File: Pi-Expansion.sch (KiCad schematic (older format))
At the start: 21 parts, among them J1 RPi_GPIO, J2 MMCX_H, J3 PINHEADER_2X2_SMD, P1 BATT, U1 A2200-A, U2 Racom R-78B5.0-1.5L

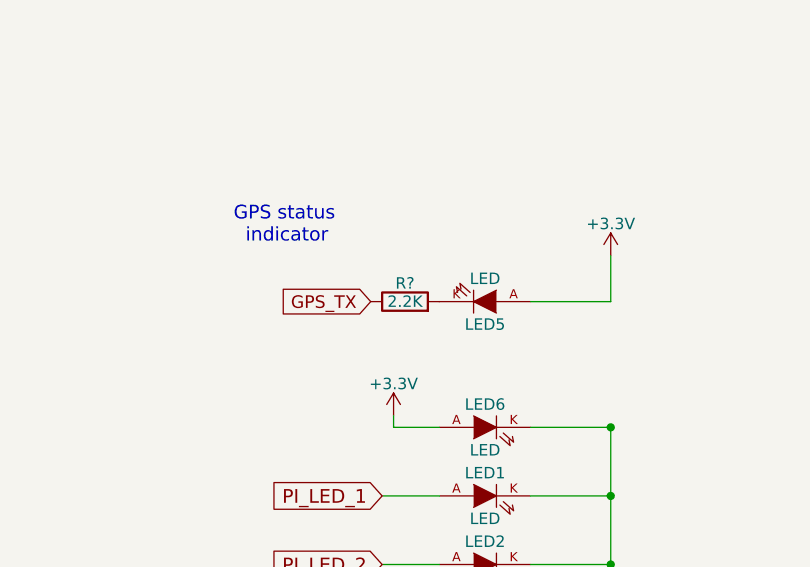
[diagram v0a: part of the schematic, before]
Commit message: Final version sent to fab, retraced GPS_TX to fix net issue between 2k2 resistor and pi header
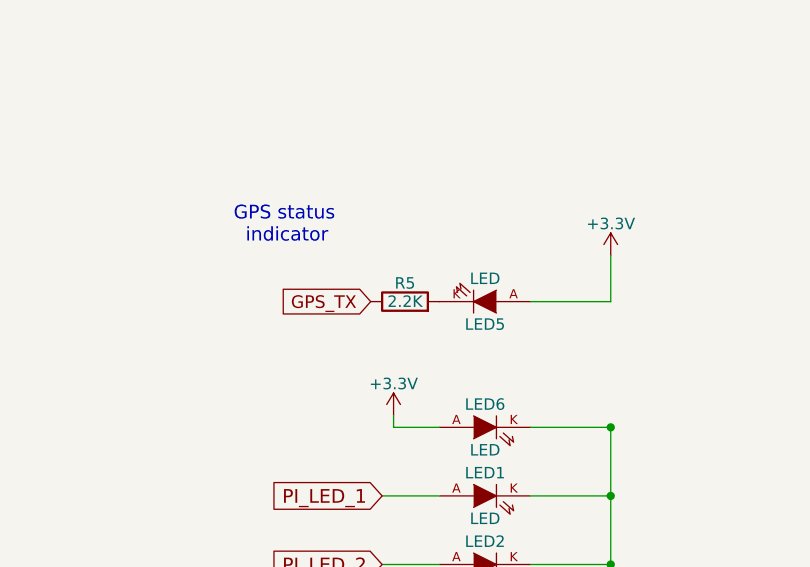
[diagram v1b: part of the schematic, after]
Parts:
- gave numbers to parts that had none: 1
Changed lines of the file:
@@
 $EndComp
 $Comp
-L GND #PWR01
+L GND #PWR18
 U 1 1 56C02961
 P 10850 5650
-F 0 "#PWR01" H 10850 5400 50  0001 C CNN
+F 0 "#PWR18" H 10850 5400 50  0001 C CNN
 F 1 "GND" H 10850 5500 50  0000 C CNN
 F 2 "" H 10850 5650 50  0000 C CNN
@@
 $EndComp
 $Comp
-L GND #PWR02
+L GND #PWR7
 U 1 1 56C0368B
 P 1350 7250
-F 0 "#PWR02" H 1350 7000 50  0001 C CNN
+F 0 "#PWR7" H 1350 7000 50  0001 C CNN
 F 1 "GND" H 1350 7100 50  0000 C CNN
 F 2 "" H 1350 7250 50  0000 C CNN
@@
 $EndComp
 $Comp
-L +3.3V #PWR03
+L +3.3V #PWR9
 U 1 1 56C03A1A
 P 2600 1100
-F 0 "#PWR03" H 2600 950 50  0001 C CNN
+F 0 "#PWR9" H 2600 950 50  0001 C CNN
 F 1 "+3.3V" H 2600 1240 50  0000 C CNN
 F 2 "" H 2600 1100 50  0000 C CNN
@@
 PI_LED_4
 $Comp
-L GND #PWR04
+L GND #PWR4
 U 1 1 56C04494
 P 1000 2950
-F 0 "#PWR04" H 1000 2700 50  0001 C CNN
+F 0 "#PWR4" H 1000 2700 50  0001 C CNN
 F 1 "GND" H 1000 2800 50  0000 C CNN
 F 2 "" H 1000 2950 50  0000 C CNN
@@
 $EndComp
 $Comp
-L +5V #PWR05
+L +5V #PWR16
 U 1 1 56C07DE9
 P 10100 1900
-F 0 "#PWR05" H 10100 1750 50  0001 C CNN
+F 0 "#PWR16" H 10100 1750 50  0001 C CNN
 F 1 "+5V" H 10100 2040 50  0000 C CNN
 F 2 "" H 10100 1900 50  0000 C CNN
@@
 	10100 1550 10100 1900
 $Comp
-L +5V #PWR06
+L +5V #PWR10
 U 1 1 56C0814E
 P 3650 5200
-F 0 "#PWR06" H 3650 5050 50  0001 C CNN
+F 0 "#PWR10" H 3650 5050 50  0001 C CNN
 F 1 "+5V" H 3650 5340 50  0000 C CNN
 F 2 "" H 3650 5200 50  0000 C CNN
@@
 	3400 5200 3650 5200
 $Comp
-L +3.3V #PWR07
+L +3.3V #PWR6
 U 1 1 56C085CB
 P 1300 5050
-F 0 "#PWR07" H 1300 4900 50  0001 C CNN
+F 0 "#PWR6" H 1300 4900 50  0001 C CNN
 F 1 "+3.3V" H 1300 5190 50  0000 C CNN
 F 2 "" H 1300 5050 50  0000 C CNN
@@
 	1300 5050 1300 5550
 $Comp
-L GND #PWR08
+L GND #PWR15
 U 1 1 56C08732
 P 9600 1900
-F 0 "#PWR08" H 9600 1650 50  0001 C CNN
+F 0 "#PWR15" H 9600 1650 50  0001 C CNN
 F 1 "GND" H 9600 1750 50  0000 C CNN
 F 2 "" H 9600 1900 50  0000 C CNN
@@
 NoConn ~ 1500 5500
 $Comp
-L GND #PWR09
+L GND #PWR1
 U 1 1 573A1DF2
 P 850 5600
-F 0 "#PWR09" H 850 5350 50  0001 C CNN
+F 0 "#PWR1" H 850 5350 50  0001 C CNN
 F 1 "GND" H 850 5450 50  0000 C CNN
 F 2 "" H 850 5600 50  0000 C CNN
@@
 $EndComp
 $Comp
-L +3.3V #PWR010
+L +3.3V #PWR2
 U 1 1 573A1E20
 P 850 6000
-F 0 "#PWR010" H 850 5850 50  0001 C CNN
+F 0 "#PWR2" H 850 5850 50  0001 C CNN
 F 1 "+3.3V" H 850 6140 50  0000 C CNN
 F 2 "" H 850 6000 50  0000 C CNN
@@
 $EndComp
 $Comp
-L GND #PWR011
+L GND #PWR5
 U 1 1 573A1E4E
 P 1250 6400
-F 0 "#PWR011" H 1250 6150 50  0001 C CNN
+F 0 "#PWR5" H 1250 6150 50  0001 C CNN
 F 1 "GND" H 1250 6250 50  0000 C CNN
 F 2 "" H 1250 6400 50  0000 C CNN
@@
 $EndComp
 $Comp
-L GND #PWR012
+L GND #PWR12
 U 1 1 573A1E7C
 P 4200 5800
-F 0 "#PWR012" H 4200 5550 50  0001 C CNN
+F 0 "#PWR12" H 4200 5550 50  0001 C CNN
 F 1 "GND" H 4200 5650 50  0000 C CNN
 F 2 "" H 4200 5800 50  0000 C CNN
@@
 $EndComp
 $Comp
-L GND #PWR013
+L GND #PWR11
 U 1 1 573A1EAA
 P 3700 6100
-F 0 "#PWR013" H 3700 5850 50  0001 C CNN
+F 0 "#PWR11" H 3700 5850 50  0001 C CNN
 F 1 "GND" H 3700 5950 50  0000 C CNN
 F 2 "" H 3700 6100 50  0000 C CNN
@@
 $EndComp
 $Comp
-L GND #PWR014
+L GND #PWR13
 U 1 1 573A1ED8
 P 4300 6800
-F 0 "#PWR014" H 4300 6550 50  0001 C CNN
+F 0 "#PWR13" H 4300 6550 50  0001 C CNN
 F 1 "GND" H 4300 6650 50  0000 C CNN
 F 2 "" H 4300 6800 50  0000 C CNN
@@
 	3700 5400 3400 5400
 $Comp
-L +3.3V #PWR015
+L +3.3V #PWR3
 U 1 1 573DF9C6
 P 1000 2150
-F 0 "#PWR015" H 1000 2000 50  0001 C CNN
+F 0 "#PWR3" H 1000 2000 50  0001 C CNN
 F 1 "+3.3V" H 1000 2290 50  0000 C CNN
 F 2 "" H 1000 2150 50  0000 C CNN
@@
 $EndComp
 $Comp
-L GND #PWR016
+L GND #PWR8
 U 1 1 573E0DA2
 P 2500 4450
-F 0 "#PWR016" H 2500 4200 50  0001 C CNN
+F 0 "#PWR8" H 2500 4200 50  0001 C CNN
 F 1 "GND" H 2500 4300 50  0000 C CNN
 F 2 "" H 2500 4450 50  0000 C CNN
@@
 Connection ~ 10100 4700
 $Comp
-L +3.3V #PWR017
+L +3.3V #PWR14
 U 1 1 573E79B2
 P 9150 4650
-F 0 "#PWR017" H 9150 4500 50  0001 C CNN
+F 0 "#PWR14" H 9150 4500 50  0001 C CNN
 F 1 "+3.3V" H 9150 4790 50  0000 C CNN
 F 2 "" H 9150 4650 50  0000 C CNN
@@
 	9150 4700 9350 4700
 $Comp
-L +3.3V #PWR018
+L +3.3V #PWR17
 U 1 1 573E8084
 P 10100 3950
-F 0 "#PWR018" H 10100 3800 50  0001 C CNN
+F 0 "#PWR17" H 10100 3800 50  0001 C CNN
 F 1 "+3.3V" H 10100 4090 50  0000 C CNN
 F 2 "" H 10100 3950 50  0000 C CNN
@@
 	9750 4150 10100 4150
 $Comp
-L R R?
+L R R5
 U 1 1 5765B84C
 P 9200 4150
-F 0 "R?" V 9280 4150 50  0000 C CNN
+F 0 "R5" V 9280 4150 50  0000 C CNN
 F 1 "2.2K" V 9200 4150 50  0000 C CNN
 F 2 "FT:1206" V 9130 4150 50  0001 C CNN

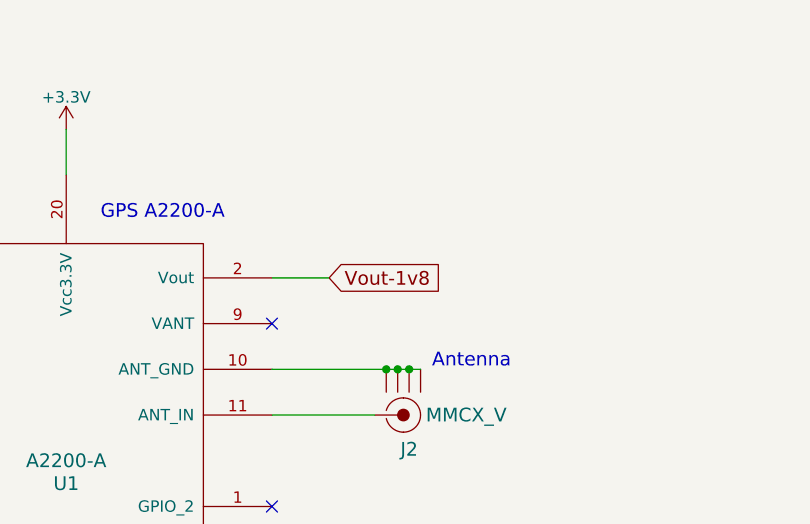
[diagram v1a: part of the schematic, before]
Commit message: Added voltage select jumper to VANT.
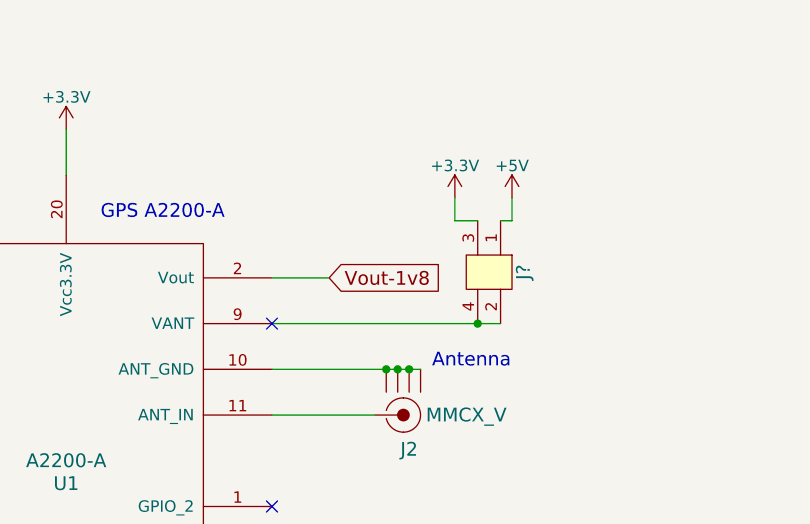
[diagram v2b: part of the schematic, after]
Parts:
- added J?: PINHEADER_2X2_SMD, Pinhead_2x2_SMD, symbol PINHEADER_2X2_SMD
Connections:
- net +3V3: now also J?.3
- net +5V: now also J?.1
- net at U1.9 (VANT): now also J?.2, J?.4
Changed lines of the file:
@@
 	0    -1   -1   0
 $EndComp
+$Comp
+L PINHEADER_2X2_SMD J?
+U 1 1 57D005ED
+P 4550 1650
+F 0 "J?" H 4625 1700 60  0000 C CNN
+F 1 "PINHEADER_2X2_SMD" H 4625 1875 60  0001 C CNN
+F 2 "Pinhead_2x2_SMD" H 4600 2000 60  0001 C CNN
+F 3 "" H 4550 1650 60  0000 C CNN
+F 4 "Digi-Key" H 4575 2450 60  0001 C CNN "Vendor"
+F 5 "WM9514-ND" H 4575 2550 60  0001 C CNN "Vendor Part Number"
+F 6 "Molex Inc" H 4600 2350 60  0001 C CNN "Manufacturer"
+F 7 "0015912040" H 4550 2225 60  0001 C CNN "Manufacturer Part Number"
+F 8 "CONN HEADER, 4POS, TIN, SMD," H 4600 2100 60  0001 C CNN "Description"
+F 9 "PinH_2X2_SMD" H 4650 1400 60  0001 C CNN "Component Value"
+	1    4550 1650
+	0    1    1    0
+$EndComp
+Wire Wire Line
+	3500 1950 4500 1950
+Connection ~ 4400 1950
+$Comp
+L +3.3V #PWR?
+U 1 1 57D00819
+P 4300 1400
+F 0 "#PWR?" H 4300 1250 50  0001 C CNN
+F 1 "+3.3V" H 4300 1540 50  0000 C CNN
+F 2 "" H 4300 1400 50  0000 C CNN
+F 3 "" H 4300 1400 50  0000 C CNN
+	1    4300 1400
+	1    0    0    -1
+$EndComp
+$Comp
+L +5V #PWR?
+U 1 1 57D00ACE
+P 4550 1400
+F 0 "#PWR?" H 4550 1250 50  0001 C CNN
+F 1 "+5V" H 4550 1540 50  0000 C CNN
+F 2 "" H 4550 1400 50  0000 C CNN
+F 3 "" H 4550 1400 50  0000 C CNN
+	1    4550 1400
+	1    0    0    -1
+$EndComp
+Wire Wire Line
+	4500 1500 4550 1500
+Wire Wire Line
+	4550 1500 4550 1400
+Wire Wire Line
+	4400 1500 4300 1500
+Wire Wire Line
+	4300 1500 4300 1400
 $EndSCHEMATC

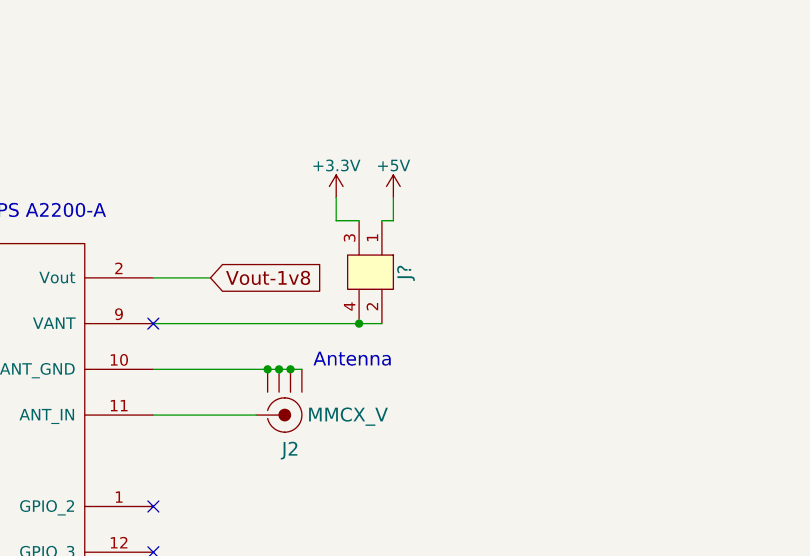
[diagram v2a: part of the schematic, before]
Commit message: Added voltage select for GPS Vant between 5v and 3v3.
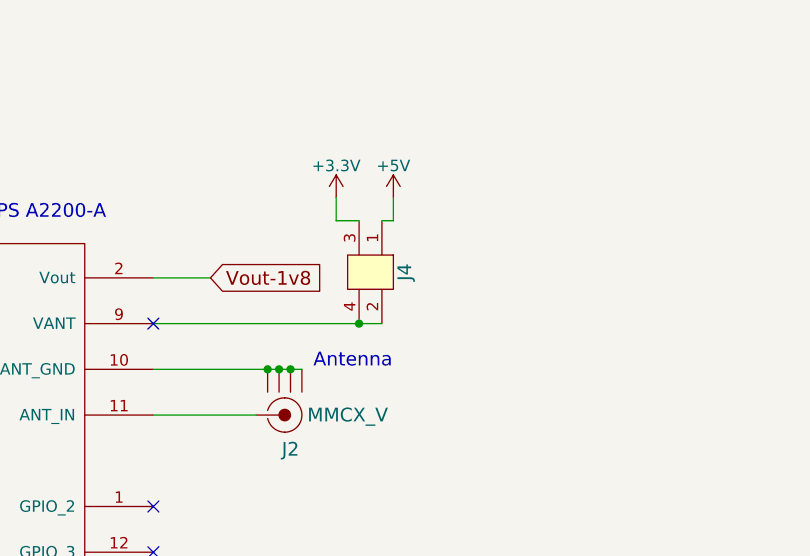
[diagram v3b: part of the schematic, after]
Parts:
- gave numbers to parts that had none: 1
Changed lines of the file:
@@
 $EndComp
 $Comp
-L GND #PWR18
+L GND #PWR20
 U 1 1 56C02961
 P 10850 5650
-F 0 "#PWR18" H 10850 5400 50  0001 C CNN
+F 0 "#PWR20" H 10850 5400 50  0001 C CNN
 F 1 "GND" H 10850 5500 50  0000 C CNN
 F 2 "" H 10850 5650 50  0000 C CNN
@@
 $EndComp
 $Comp
-L +5V #PWR16
+L +5V #PWR18
 U 1 1 56C07DE9
 P 10100 1900
-F 0 "#PWR16" H 10100 1750 50  0001 C CNN
+F 0 "#PWR18" H 10100 1750 50  0001 C CNN
 F 1 "+5V" H 10100 2040 50  0000 C CNN
 F 2 "" H 10100 1900 50  0000 C CNN
@@
 	1300 5050 1300 5550
 $Comp
-L GND #PWR15
+L GND #PWR17
 U 1 1 56C08732
 P 9600 1900
-F 0 "#PWR15" H 9600 1650 50  0001 C CNN
+F 0 "#PWR17" H 9600 1650 50  0001 C CNN
 F 1 "GND" H 9600 1750 50  0000 C CNN
 F 2 "" H 9600 1900 50  0000 C CNN
@@
 $EndComp
 $Comp
-L GND #PWR13
+L GND #PWR14
 U 1 1 573A1ED8
 P 4300 6800
-F 0 "#PWR13" H 4300 6550 50  0001 C CNN
+F 0 "#PWR14" H 4300 6550 50  0001 C CNN
 F 1 "GND" H 4300 6650 50  0000 C CNN
 F 2 "" H 4300 6800 50  0000 C CNN
@@
 Connection ~ 10100 4700
 $Comp
-L +3.3V #PWR14
+L +3.3V #PWR16
 U 1 1 573E79B2
 P 9150 4650
-F 0 "#PWR14" H 9150 4500 50  0001 C CNN
+F 0 "#PWR16" H 9150 4500 50  0001 C CNN
 F 1 "+3.3V" H 9150 4790 50  0000 C CNN
 F 2 "" H 9150 4650 50  0000 C CNN
@@
 	9150 4700 9350 4700
 $Comp
-L +3.3V #PWR17
+L +3.3V #PWR19
 U 1 1 573E8084
 P 10100 3950
-F 0 "#PWR17" H 10100 3800 50  0001 C CNN
+F 0 "#PWR19" H 10100 3800 50  0001 C CNN
 F 1 "+3.3V" H 10100 4090 50  0000 C CNN
 F 2 "" H 10100 3950 50  0000 C CNN
@@
 $EndComp
 $Comp
-L PINHEADER_2X2_SMD J?
+L PINHEADER_2X2_SMD J4
 U 1 1 57D005ED
 P 4550 1650
-F 0 "J?" H 4625 1700 60  0000 C CNN
+F 0 "J4" H 4625 1700 60  0000 C CNN
 F 1 "PINHEADER_2X2_SMD" H 4625 1875 60  0001 C CNN
 F 2 "Pinhead_2x2_SMD" H 4600 2000 60  0001 C CNN
@@
 Connection ~ 4400 1950
 $Comp
-L +3.3V #PWR?
+L +3.3V #PWR13
 U 1 1 57D00819
 P 4300 1400
-F 0 "#PWR?" H 4300 1250 50  0001 C CNN
+F 0 "#PWR13" H 4300 1250 50  0001 C CNN
 F 1 "+3.3V" H 4300 1540 50  0000 C CNN
 F 2 "" H 4300 1400 50  0000 C CNN
@@
 $EndComp
 $Comp
-L +5V #PWR?
+L +5V #PWR15
 U 1 1 57D00ACE
 P 4550 1400
-F 0 "#PWR?" H 4550 1250 50  0001 C CNN
+F 0 "#PWR15" H 4550 1250 50  0001 C CNN
 F 1 "+5V" H 4550 1540 50  0000 C CNN
 F 2 "" H 4550 1400 50  0000 C CNN
